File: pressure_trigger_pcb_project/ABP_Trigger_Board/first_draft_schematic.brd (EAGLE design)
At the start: 100 x 80 mm, 27 parts, among them U1 AD5206BRUZ10, U2 OPA4340UA

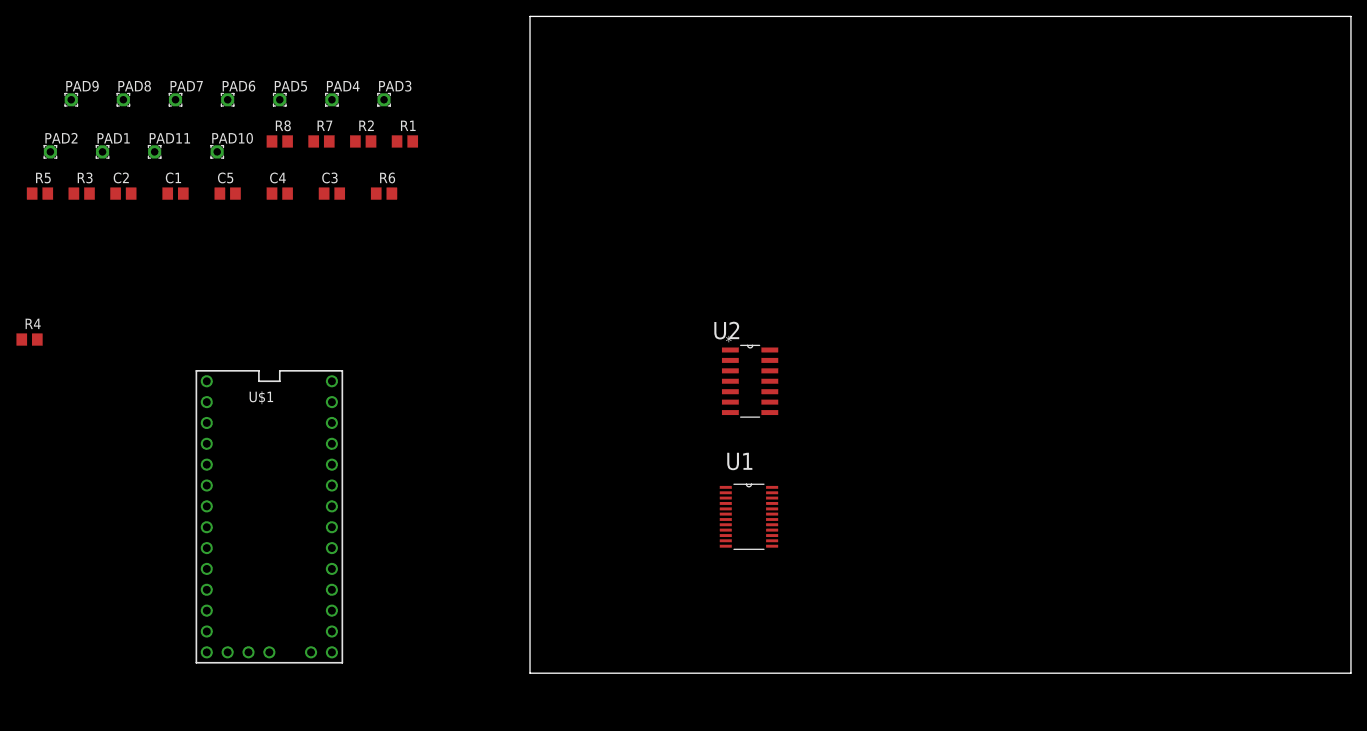
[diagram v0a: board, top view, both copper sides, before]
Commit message: routed REV A of the board, silkscreen not yet done
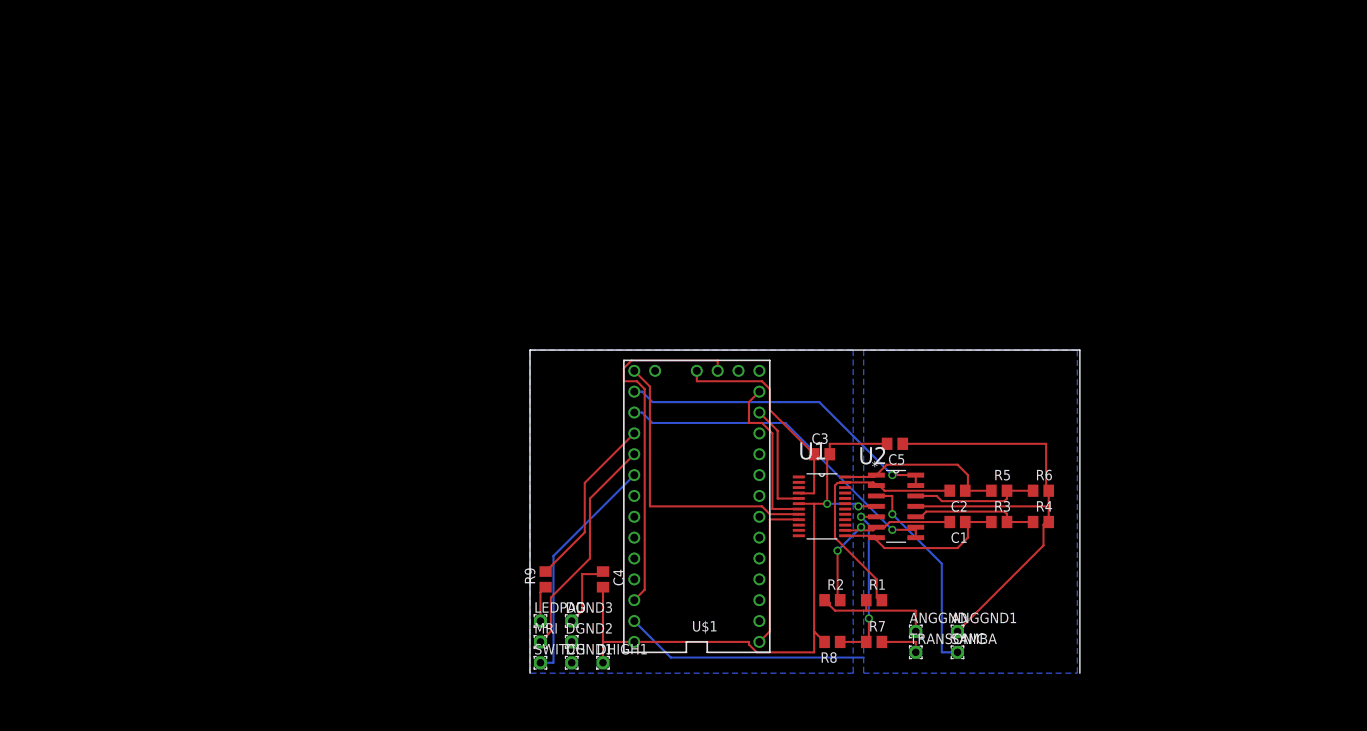
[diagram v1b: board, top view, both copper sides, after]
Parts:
- removed PAD1, PAD10, PAD11, PAD2, PAD3, PAD4, PAD5, PAD6, PAD7, PAD8, PAD9: WIREPAD1,6/0,9, wirepad:1,6/0,9
- added ANGGND, ANGGND1, DGND1, DGND2, DGND3, DHIGH1, LEDPAD, MRI, SWITCH, TRANSONIC: WIREPAD1,6/0,9, wirepad:1,6/0,9
- added R9: 681, resistor:R0805
- added SAMBA: SAMBA, wirepad:1,6/0,9
- R7, R8: value 5k -> 10k
- moved R4 125.2 mm to (62.2, 18.4)
- moved R5 122.3 mm to (57.1, 22.2)
- moved R3 118.7 mm to (57.1, 18.4)
- moved C2 107.9 mm to (52.1, 22.2), turned to 180 degrees
- moved C1 103.3 mm to (52.1, 18.4), turned to 180 degrees
- moved R7 90.8 mm to (41.9, 3.81)
- moved R8 90.8 mm to (36.8, 3.81), turned to 180 degrees
- moved R6 87.8 mm to (62.2, 22.2)
- moved C5 86.8 mm to (44.5, 27.9), turned to 180 degrees
- moved R1 79.9 mm to (41.9, 8.89)
- moved R2 79.9 mm to (36.8, 8.89)
- moved C3 67.6 mm to (35.6, 26.7)
- moved C4 61.3 mm to (8.89, 11.4), turned to 270 degrees
- moved U$1 52.1 mm to (20.3, 20.3), turned to 180 degrees
- moved U2 23.4 mm to (47.0, 16.5)
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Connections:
- new net N$9: R3.2, R4.1, U2.10
- net AGND: now also ANGGND.1, ANGGND1.1, C5.1, R1.1, R2.1, R4.2, R6.2, U2.11
- net GND: now also DGND1.1, DGND2.1, DGND3.1, U1.9; no longer C5.1, PAD11.1, PAD3.1, PAD4.1, PAD7.1, PAD9.1, R1.1, R2.1, R4.2, R6.2, U1.6, U2.11
- net N$1: now also U2.13, U2.14; no longer U2.6, U2.7
- net N$10: now also SAMBA.1, U2.3; no longer R5.2, R6.1, U2.5
- net N$11: now also LEDPAD.1, R9.1; no longer R3.2, R4.1, U2.12
- net N$12: now also C1.2, R2.2, U1.14, U2.6; no longer PAD1.1, U2.3
- net N$13: now also TRANSONIC.1; no longer PAD2.1
- net N$14: now also R9.2; no longer PAD10.1
- net N$15: now also MRI.1; no longer PAD8.1
- net N$16: now also SWITCH.1; no longer PAD5.1
- net N$17: now also C1.1, R3.1, U1.13, U2.7; no longer R7.1, R8.1, U2.10
- net N$2: now also U$1.15/A1, U2.8; no longer C2.2, R2.2, U1.16
- net N$3: now also C2.2, R1.2, U1.23, U2.2; no longer U$1.15/A1, U2.13, U2.14
- net N$4: now also R7.1, R8.1, U2.5; no longer C1.1, R5.1, U1.20, U2.1
- net N$5: now also R5.1, U1.24, U2.1; no longer R3.1, U1.17, U2.8
- net N$6: now also R5.2, R6.1, U2.12; no longer C1.2, R1.2, U1.21, U2.2
- net VCC: now also DHIGH1.1, U1.6; no longer PAD6.1, U1.9
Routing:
- net AGND: track 0.00 -> 107.0 mm
- net VCC: track 0.00 -> 79.7 mm, vias 0 -> 2
- net GND: track 0.00 -> 55.5 mm
- net 3.3V: track 0.00 -> 43.9 mm
- net N$2: track 0.00 -> 41.5 mm, vias 0 -> 1
- net N$1: track 0.00 -> 39.8 mm, vias 0 -> 1
- net N$19: track 0.00 -> 35.8 mm
- net N$3: track 0.00 -> 31.1 mm
- net N$16: track 0.00 -> 28.5 mm
- net N$15: track 0.00 -> 27.6 mm
- net N$10: track 0.00 -> 25.4 mm, vias 0 -> 1
- net N$12: track 0.00 -> 23.9 mm, vias 0 -> 2
- net N$17: track 0.00 -> 21.5 mm
- net N$5: track 0.00 -> 21.3 mm
- net N$14: track 0.00 -> 21.3 mm
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- added copper zone on layer 16, net AGND
- added copper zone on layer 16, net GND
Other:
- board size 100 x 80 mm -> 67 x 39.4 mm

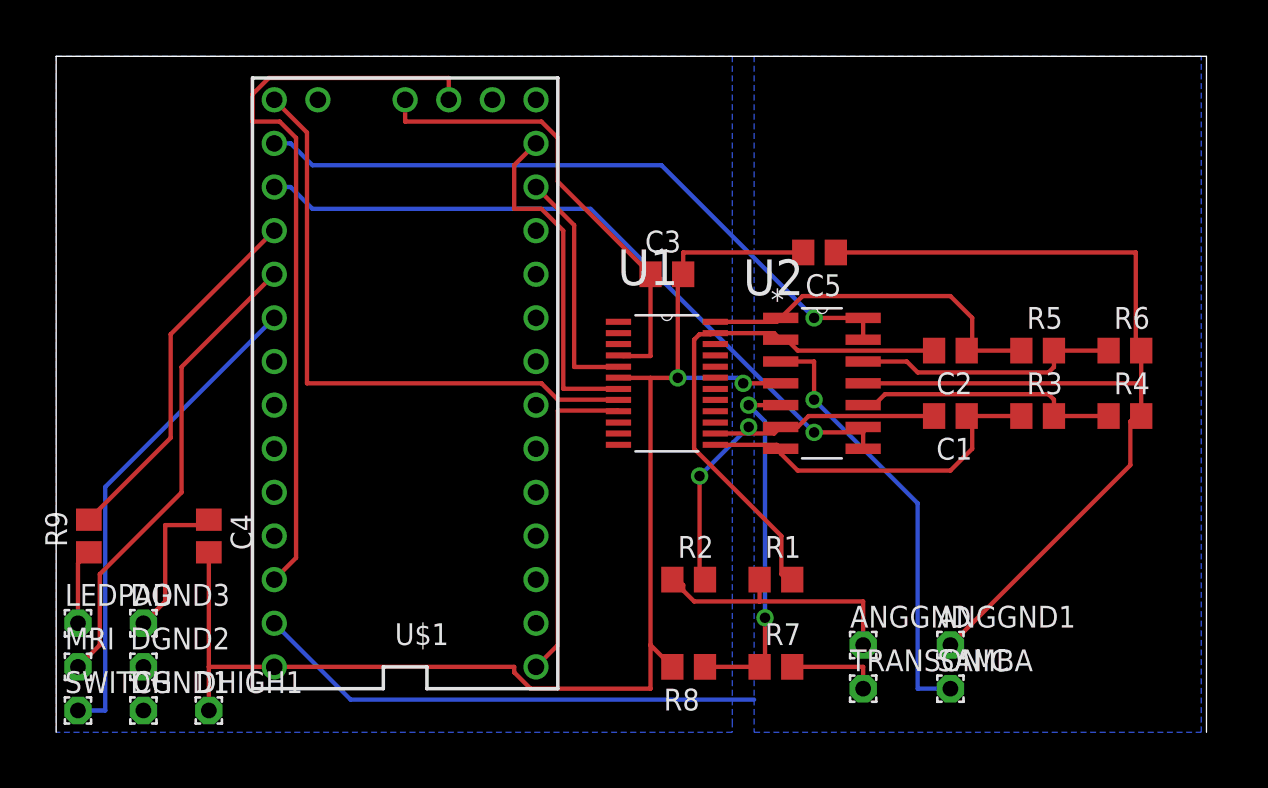
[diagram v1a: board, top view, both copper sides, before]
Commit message: updated board fixed labels
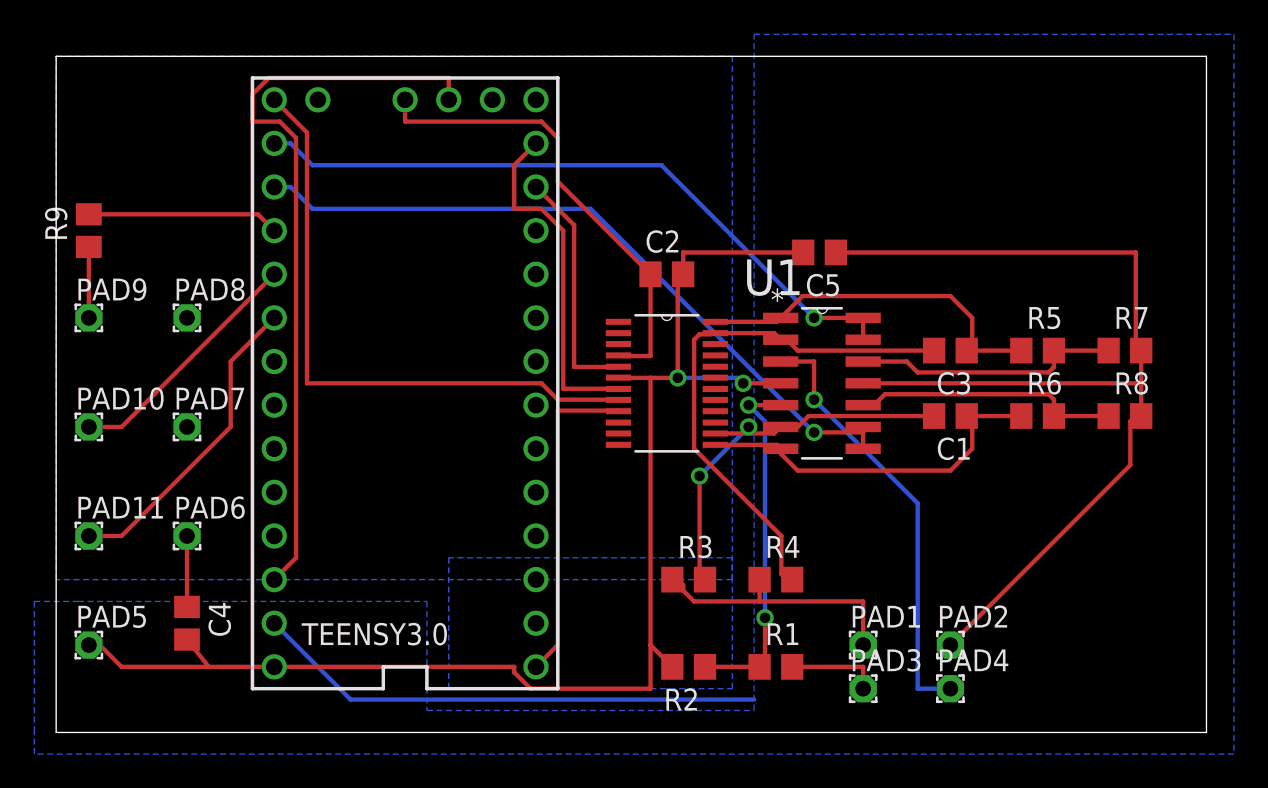
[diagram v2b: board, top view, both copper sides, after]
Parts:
- removed DGND1, DGND2, DGND3, DHIGH1, LEDPAD, MRI, SWITCH: WIREPAD1,6/0,9, wirepad:1,6/0,9
- removed U2: OPA4340UA, Texas Instruments_By_element14_Batch_1:SOIC127P600X175-14N
- added AD5206: AD5206BRUZ10, AD5206:SOP65P640X120-24N
- added PAD10, PAD11, PAD5, PAD6, PAD7, PAD8, PAD9: WIREPAD1,6/0,9, wirepad:1,6/0,9
- C2: value 10pF -> 0.1uF
- C3: value 0.1uF -> 10pF
- R1, R2: value 5k -> 10k
- R3: value 12k -> 5k
- R4: value 23.2k -> 5k
- R6: value 23.2k -> 12k
- R7, R8: value 10k -> 23.2k
- U1: value AD5206BRUZ10 -> OPA4340UA; device AD5206:SOP65P640X120-24N -> Texas Instruments_By_element14_Batch_1:SOIC127P600X175-14N
- moved R8 29.3 mm to (62.2, 18.4), turned to 0 degrees
- moved R7 27.4 mm to (62.2, 22.2)
- moved R3 22.4 mm to (36.8, 8.89)
- moved R4 22.4 mm to (41.9, 8.89)
- moved R9 17.8 mm to (1.91, 29.2)
- moved C2 17.1 mm to (35.6, 26.7), turned to 0 degrees
- moved C3 17.1 mm to (52.1, 22.2), turned to 180 degrees
- moved U1 12.0 mm to (47.0, 16.5)
- moved R6 6.35 mm to (57.1, 18.4)
- moved C4 5.24 mm to (7.62, 6.35)
- moved R1 5.08 mm to (41.9, 3.81)
- moved R2 5.08 mm to (36.8, 3.81), turned to 180 degrees
- renumbered ANGGND to PAD1, ANGGND1 to PAD2, SAMBA to PAD4, TRANSONIC to PAD3, U$1 to TEENSY3.0
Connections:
- net AGND: now also R3.1, R4.1, R7.2, R8.2, U1.11; no longer R1.1, R2.1, R4.2, R6.2, U2.11
- net GND: now also AD5206.4, AD5206.9, C2.1, PAD6.1, PAD7.1, PAD8.1; no longer C3.1, DGND1.1, DGND2.1, DGND3.1, U1.4, U1.9
- net N$1: now also U1.13, U1.14; no longer U2.13, U2.14
- net N$10: now also U1.3; no longer U2.3
- net N$11: now also PAD9.1; no longer LEDPAD.1
- net N$12: now also AD5206.14, R3.2, U1.6; no longer R2.2, U1.14, U2.6
- net N$13: now also R1.2; no longer R7.2
- net N$15: now also PAD10.1; no longer MRI.1
- net N$16: now also PAD11.1; no longer SWITCH.1
- net N$17: now also AD5206.13, R6.1, U1.7; no longer R3.1, U1.13, U2.7
- net N$19: now also AD5206.8; no longer U1.8
- net N$2: now also U1.8, U1.9; no longer U2.8, U2.9
- net N$3: now also AD5206.23, C3.2, R4.2, U1.2; no longer C2.2, R1.2, U1.23, U2.2
- net N$4: now also R1.1, R2.1, U1.5; no longer R7.1, R8.1, U2.5
- net N$5: now also AD5206.24, C3.1, U1.1; no longer C2.1, U1.24, U2.1
- net N$6: now also R7.1, U1.12; no longer R6.1, U2.12
- net N$7: now also AD5206.5; no longer U1.5
- net N$8: now also AD5206.7; no longer U1.7
- net N$9: now also R6.2, R8.1, U1.10; no longer R3.2, R4.1, U2.10
- net VCC: now also AD5206.6, C2.2, PAD5.1, R2.2, U1.4; no longer C3.2, DHIGH1.1, R8.2, U1.6, U2.4
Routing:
- net N$15: track 27.6 -> 14.5 mm
- net N$16: track 28.5 -> 18.3 mm
- net N$14: track 21.3 -> 11.2 mm
- net GND: track 55.5 -> 50.5 mm

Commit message: new board layout
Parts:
- removed AD5206: AD5206BRUZ10, AD5206:SOP65P640X120-24N
- removed PAD1, PAD10, PAD11, PAD2, PAD3, PAD5, PAD9: WIREPAD1,6/0,9, wirepad:1,6/0,9
- removed PAD4: SAMBA, wirepad:1,6/0,9
- added AD5206-50: AD5206BRUZ10, AD5206:SOP65P640X120-24N
- added DH, LED, MRI, SEL, SG, TC, TG: WIREPAD1,6/0,9, wirepad:1,6/0,9
- added SB: SAMBA, wirepad:1,6/0,9
- moved R2 32.4 mm to (61.0, 25.4)
- moved R1 26.1 mm to (61.0, 21.6)
- moved R9 22.5 mm to (24.1, 26.0), turned to 270 degrees
- moved R7 21.9 mm to (41.9, 14.0)
- moved C2 21.1 mm to (43.2, 6.99), turned to 90 degrees
- moved C4 20.1 mm to (3.81, 26.0)
- moved R3 18.5 mm to (54.6, 14.0)
- moved PAD6 17.4 mm to (10.8, 28.6), turned to 270 degrees
- moved C5 16.6 mm to (61.0, 29.2)
- moved R5 15.9 mm to (41.9, 17.8), turned to 180 degrees
- moved U1 13.1 mm to (55.2, 26.7), turned to 90 degrees
- moved PAD7 12.9 mm to (14.6, 28.6), turned to 270 degrees
- moved PAD8 11.7 mm to (18.4, 28.6), turned to 270 degrees
- moved TEENSY3.0 8.28 mm to (19.7, 12.1), turned to 90 degrees
- moved R4 8.13 mm to (48.3, 14.0), turned to 180 degrees
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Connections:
- net AGND: now also SG.1, TG.1; no longer PAD1.1, PAD2.1
- net GND: now also AD5206-50.4, AD5206-50.9; no longer AD5206.4, AD5206.9
- net N$1: now also TEENSY3.0.15/A1; no longer TEENSY3.0.14/A0
- net N$10: now also SB.1; no longer PAD4.1
- net N$11: now also LED.1; no longer PAD9.1
- net N$12: now also AD5206-50.14; no longer AD5206.14
- net N$13: now also TC.1; no longer PAD3.1
- net N$15: now also MRI.1; no longer PAD10.1
- net N$16: now also SEL.1; no longer PAD11.1
- net N$17: now also AD5206-50.13; no longer AD5206.13
- net N$19: now also AD5206-50.8; no longer AD5206.8
- net N$2: now also TEENSY3.0.14/A0; no longer TEENSY3.0.15/A1
- net N$3: now also AD5206-50.23; no longer AD5206.23
- net N$5: now also AD5206-50.24; no longer AD5206.24
- net N$7: now also AD5206-50.5; no longer AD5206.5
- net N$8: now also AD5206-50.7; no longer AD5206.7
- net VCC: now also AD5206-50.6, DH.1; no longer AD5206.6, PAD5.1
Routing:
- net AGND: track 107.0 -> 18.2 mm, vias 0 -> 4
- net VCC: track 80.1 -> 149.3 mm
- net GND: track 50.5 -> 19.9 mm, vias 0 -> 2
- net N$1: track 39.8 -> 20.7 mm, vias 1 -> 0
- net N$3: track 31.1 -> 13.2 mm
- net 3.3V: track 43.9 -> 32.1 mm
- net N$2: track 41.5 -> 30.3 mm, vias 1 -> 2
- net N$9: track 15.6 -> 26.7 mm, vias 0 -> 2
- net N$12: track 23.9 -> 14.0 mm, vias 2 -> 0
- net N$19: track 35.8 -> 27.0 mm
- net N$10: track 25.4 -> 17.3 mm, vias 1 -> 0
- net N$7: track 14.0 -> 22.0 mm
- net N$4: track 21.0 -> 25.6 mm, vias 2 -> 0
- net N$14: track 11.2 -> 7.24 mm
- net N$5: track 21.3 -> 17.5 mm
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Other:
- board size 67 x 39.4 mm -> 67.6 x 33 mm
- board text added: "ARTERIAL BP TRIGGERING SYSTEM REV B JOSHBRADSHAW11@GMAIL.COM"

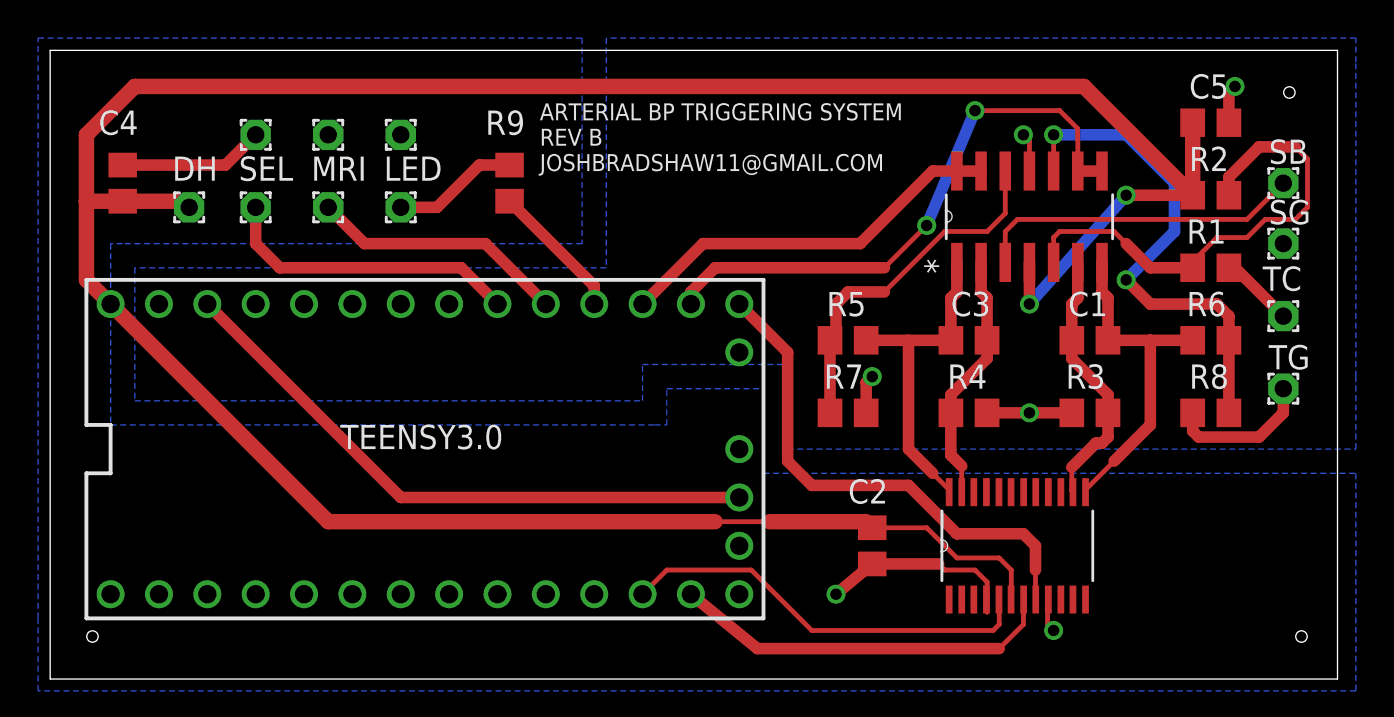
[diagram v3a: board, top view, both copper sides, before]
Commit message: made finishing touching to the boards silkscreen and fattenned up the traces where I could
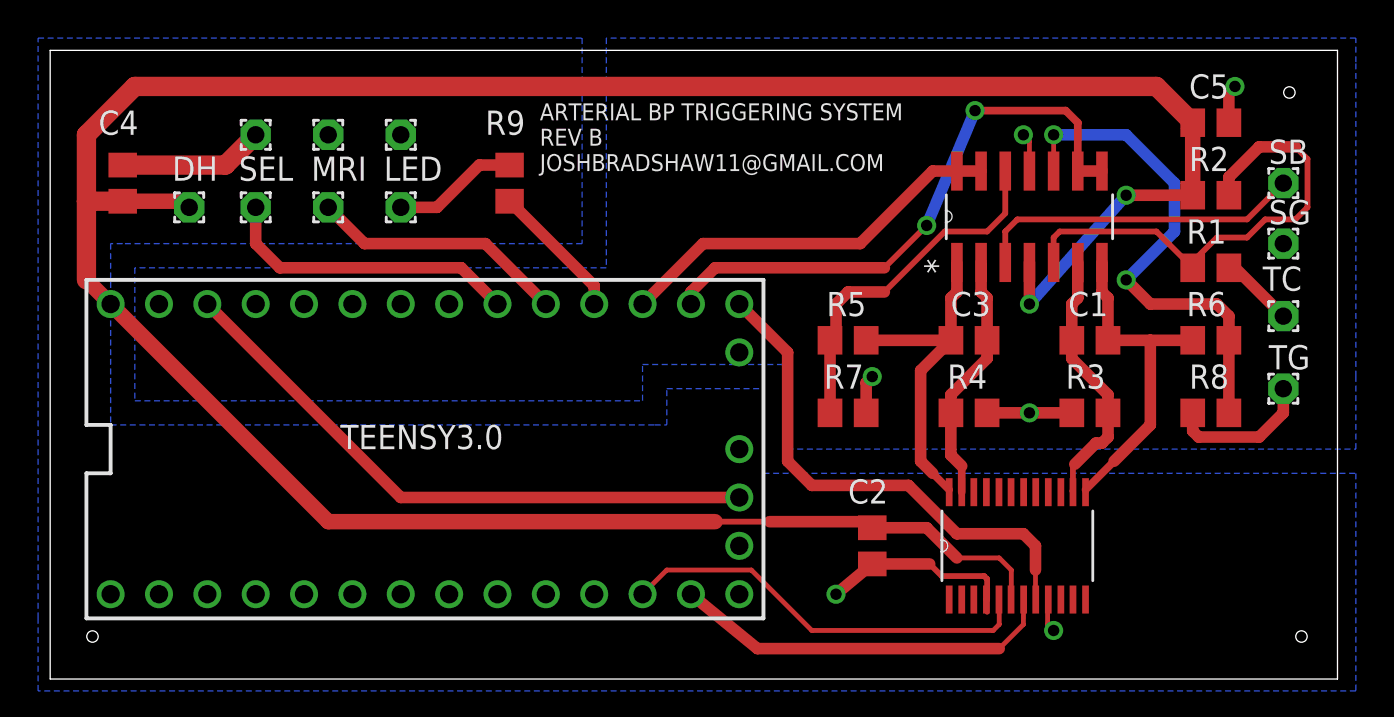
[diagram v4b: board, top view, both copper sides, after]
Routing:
- net VCC: track 149.3 -> 147.7 mm
- net GND: track 19.9 -> 20.7 mm
